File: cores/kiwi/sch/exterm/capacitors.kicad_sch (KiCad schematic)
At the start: 27 parts

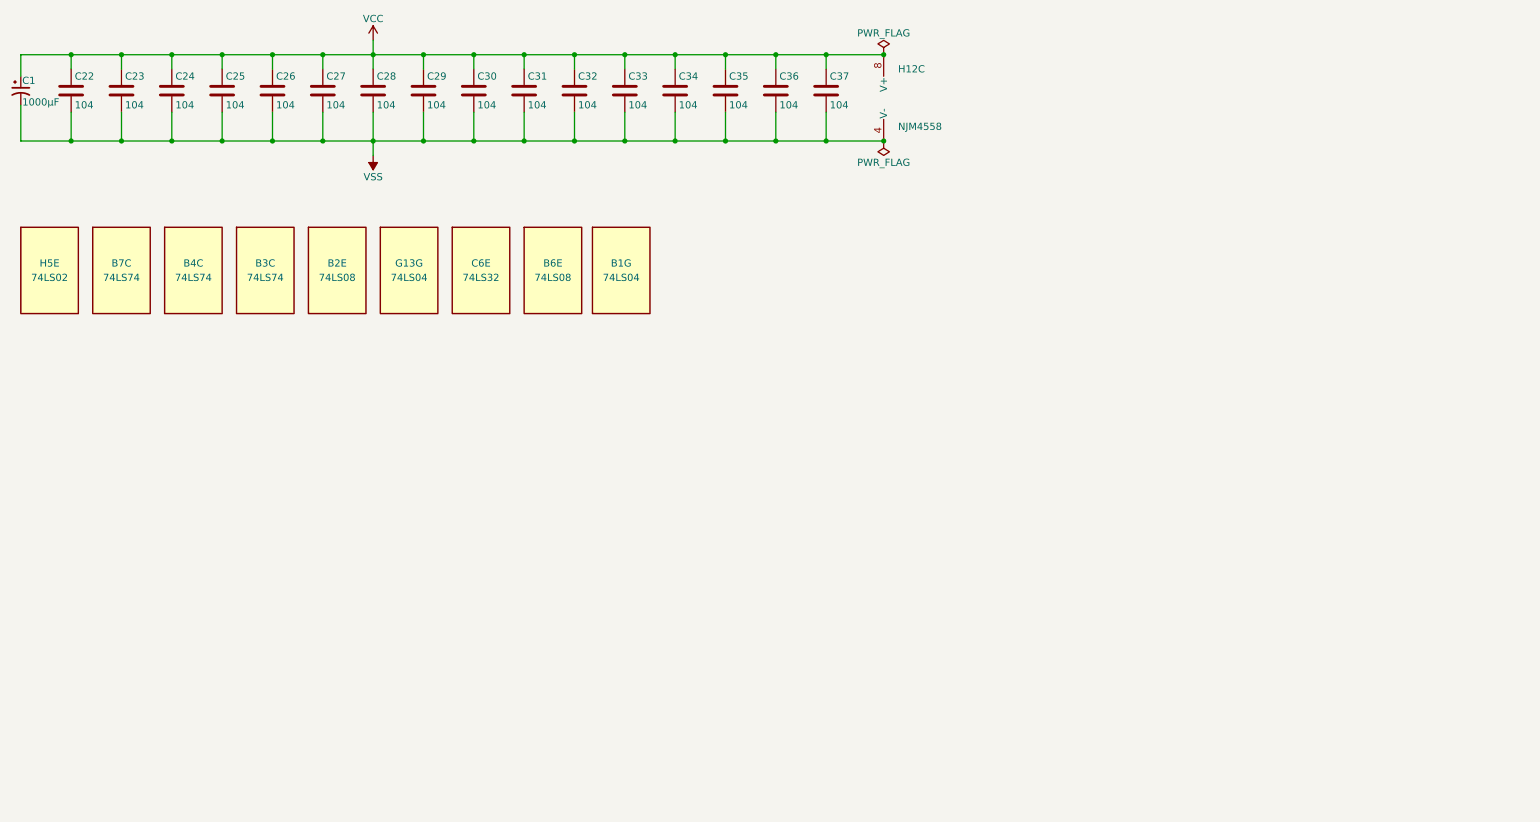
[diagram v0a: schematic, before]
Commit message: sheet_size_update
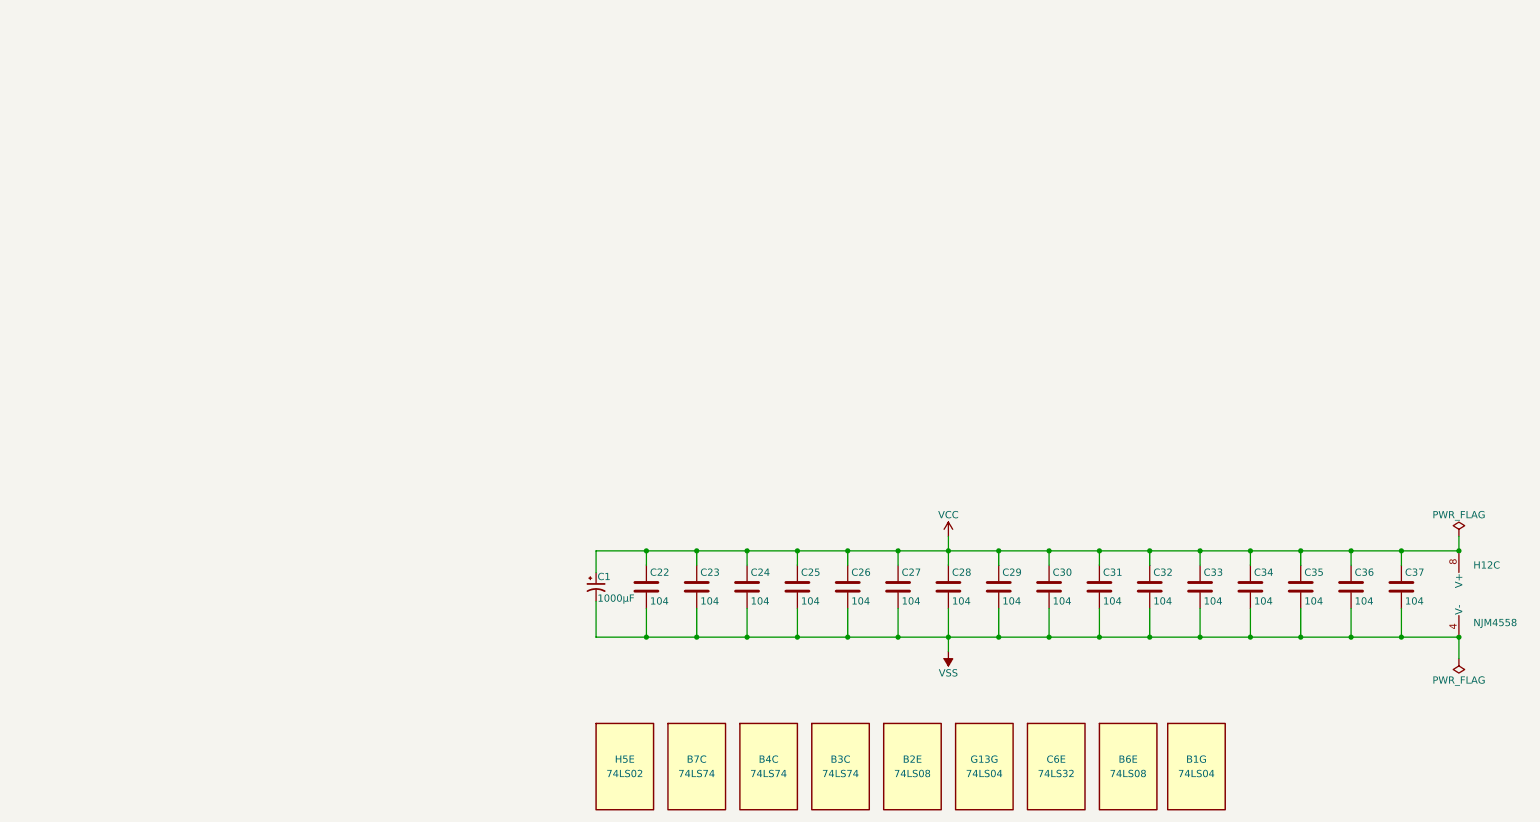
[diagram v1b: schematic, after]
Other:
- moved on the sheet: B1G, B2E, B3C, B4C, B6E, B7C, C1, C22, C23, C24, C25, C26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
